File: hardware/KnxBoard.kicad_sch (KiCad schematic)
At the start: 40 parts, among them J1 Conn_01x10, J2 Conn_01x12, J3 Conn_01x12, J4 Conn_01x02_Male, U1 NCN5130, U3 STM32L432KCUx, X1 FA-238

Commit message: Start new schematics
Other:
- sheet MCU ports: added DEBUG_JTCK-SWCLK, DEBUG_JTDA-SWO, DEBUG_JTDI, DEBUG_JTMS-SWDIO, DEBUG_UART_RX, DEBUG_UART_TX, KNX_PROG_BTN, KNX_PROG_LED, KNX_RESETB, KNX_SAVEB, KNX_UART_RX, KNX_UART_TX, NRST, RCC_OSC_IN; removed none
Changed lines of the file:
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@@
     (pin "2")
   )
-  (sheet (at 231.14 137.16) (size 31.75 19.05) (fields_autoplaced)
+  (sheet (at 130.81 142.24) (size 39.37 35.56) (fields_autoplaced)
     (stroke (width 0.1524) (type solid) (color 0 0 0 0))
     (fill (color 0 0 0 0.0000))
-    (property "Sheet name" "MCU" (id 0) (at 231.14 136.4484 0)
+    (property "Sheet name" "MCU" (id 0) (at 130.81 141.5284 0)
       (effects (font (size 1.27 1.27)) (justify left bottom))
     )
-    (property "Sheet file" "mcu.kicad_sch" (id 1) (at 231.14 156.7946 0)
+    (property "Sheet file" "mcu.kicad_sch" (id 1) (at 130.81 178.3846 0)
       (effects (font (size 1.27 1.27)) (justify left top))
+    )
+    (pin "DEBUG_JTDI" input (at 170.18 146.05 0)
+      (effects (font (size 1.27 1.27)) (justify right))
+    )
+    (pin "KNX_UART_TX" output (at 130.81 146.05 180)
+      (effects (font (size 1.27 1.27)) (justify left))
+    )
+    (pin "KNX_UART_RX" input (at 130.81 149.86 180)
+      (effects (font (size 1.27 1.27)) (justify left))
+    )
+    (pin "DEBUG_UART_TX" output (at 170.18 165.1 0)
+      (effects (font (size 1.27 1.27)) (justify right))
+    )
+    (pin "DEBUG_UART_RX" input (at 170.18 161.29 0)
+      (effects (font (size 1.27 1.27)) (justify right))
+    )
+    (pin "DEBUG_JTMS-SWDIO" bidirectional (at 170.18 149.86 0)
+      (effects (font (size 1.27 1.27)) (justify right))
+    )
+    (pin "DEBUG_JTCK-SWCLK" input (at 170.18 153.67 0)
+      (effects (font (size 1.27 1.27)) (justify right))
+    )
+    (pin "DEBUG_JTDA-SWO" output (at 170.18 157.48 0)
+      (effects (font (size 1.27 1.27)) (justify right))
+    )
+    (pin "RCC_OSC_IN" input (at 130.81 153.67 180)
+      (effects (font (size 1.27 1.27)) (justify left))
+    )
+    (pin "KNX_PROG_BTN" input (at 130.81 165.1 180)
+      (effects (font (size 1.27 1.27)) (justify left))
+    )
+    (pin "KNX_PROG_LED" output (at 130.81 168.91 180)
+      (effects (font (size 1.27 1.27)) (justify left))
+    )
+    (pin "KNX_SAVEB" input (at 130.81 157.48 180)
+      (effects (font (size 1.27 1.27)) (justify left))
+    )
+    (pin "NRST" input (at 130.81 175.26 180)
+      (effects (font (size 1.27 1.27)) (justify left))
+    )
+    (pin "KNX_RESETB" input (at 130.81 161.29 180)
+      (effects (font (size 1.27 1.27)) (justify left))
     )
   )
@@
       (reference "#PWR0124") (unit 1) (value "+3.3V") (footprint "")
     )
+    (path "/d8441614-dec4-4bc1-b184-c502a3d79ed5/03d27323-09b9-4b11-a017-9b5707a4dd98"
+      (reference "#PWR?") (unit 1) (value "GNDREF") (footprint "")
+    )
+    (path "/d8441614-dec4-4bc1-b184-c502a3d79ed5/0e9598fb-406f-4d4d-b9a8-c71195fe8ca0"
+      (reference "#PWR?") (unit 1) (value "+3.3V") (footprint "")
+    )
+    (path "/d8441614-dec4-4bc1-b184-c502a3d79ed5/3343c915-cf9e-405b-b8b0-f09759c8714d"
+      (reference "#PWR?") (unit 1) (value "GNDREF") (footprint "")
+    )
+    (path "/d8441614-dec4-4bc1-b184-c502a3d79ed5/3be508aa-8a93-4fde-9c22-a5b8008e5c2e"
+      (reference "#PWR?") (unit 1) (value "GNDREF") (footprint "")
+    )
+    (path "/d8441614-dec4-4bc1-b184-c502a3d79ed5/7b38bb45-3f6f-4e1e-a07e-f7739b04601c"
+      (reference "#PWR?") (unit 1) (value "+3.3V") (footprint "")
+    )
+    (path "/d8441614-dec4-4bc1-b184-c502a3d79ed5/a6da1779-828c-48b4-a087-8262a42e5001"
+      (reference "#PWR?") (unit 1) (value "GNDREF") (footprint "")
+    )
+    (path "/d8441614-dec4-4bc1-b184-c502a3d79ed5/b25d33ec-3885-48d4-84ad-c25564664654"
+      (reference "#PWR?") (unit 1) (value "GNDREF") (footprint "")
+    )
+    (path "/d8441614-dec4-4bc1-b184-c502a3d79ed5/0dea2631-b9f1-4451-83e1-0bf67fac2912"
+      (reference "B1") (unit 1) (value "Reset") (footprint "")
+    )
     (path "/00000000-0000-0000-0000-00006184f7b9"
       (reference "C1") (unit 1) (value "47nF 50V") (footprint "Capacitor_SMD:C_0603_1608Metric")
@@
       (reference "C2") (unit 1) (value "220nF 50V") (footprint "Capacitor_SMD:C_0603_1608Metric")
     )
+    (path "/d8441614-dec4-4bc1-b184-c502a3d79ed5/ed583750-47fe-4327-89c8-ba86b7af17a1"
+      (reference "C2") (unit 1) (value "10uF") (footprint "")
+    )
     (path "/00000000-0000-0000-0000-0000618508bd"
       (reference "C3") (unit 1) (value "100nF 50V") (footprint "Capacitor_SMD:C_0603_1608Metric")
     )
+    (path "/d8441614-dec4-4bc1-b184-c502a3d79ed5/de02d626-c6a9-4a11-a470-5f7c3b547a04"
+      (reference "C3_25") (unit 1) (value "100nF") (footprint "")
+    )
+    (path "/d8441614-dec4-4bc1-b184-c502a3d79ed5/933de220-4835-475e-b429-30ce2da9a7e1"
+      (reference "C3_36") (unit 1) (value "100nF") (footprint "")
+    )
+    (path "/d8441614-dec4-4bc1-b184-c502a3d79ed5/f1ce25fb-e741-4020-b5e8-a7f4df1b610b"
+      (reference "C3_48") (unit 1) (value "100nF") (footprint "")
+    )
     (path "/00000000-0000-0000-0000-00006186317f"
       (reference "C4") (unit 1) (value "100uF 35V") (footprint "Capacitor_SMD:CP_Elec_6.3x7.7")
     )
+    (path "/d8441614-dec4-4bc1-b184-c502a3d79ed5/48cdbdf2-3cea-4abb-8f0a-a74466c9c644"
+      (reference "C4") (unit 1) (value "1uF") (footprint "")
+    )
     (path "/00000000-0000-0000-0000-00006186f111"
       (reference "C5") (unit 1) (value "100nF 6.3V") (footprint "Capacitor_SMD:C_0603_1608Metric")
     )
+    (path "/d8441614-dec4-4bc1-b184-c502a3d79ed5/97e619e0-9643-4a02-b982-345810d00de5"
+      (reference "C5_9") (unit 1) (value "100nF") (footprint "")
+    )
     (path "/00000000-0000-0000-0000-00006186bb40"
       (reference "C6") (unit 1) (value "100nF 6.3V") (footprint "Capacitor_SMD:C_0603_1608Metric")
@@
       (reference "C11") (unit 1) (value "10uF 6.3V ESR < 0.1ohm") (footprint "Capacitor_SMD:C_0805_2012Metric")
     )
+    (path "/d8441614-dec4-4bc1-b184-c502a3d79ed5/96b13407-7e12-4054-b229-f3f0cc548ef8"
+      (reference "C17") (unit 1) (value "100 nF") (footprint "")
+    )
     (path "/00000000-0000-0000-0000-0000619333de"
       (reference "C20") (unit 1) (value "100nF 6.3V") (footprint "Capacitor_SMD:C_0603_1608Metric")
@@
       (reference "C41") (unit 1) (value "1uF 35V ESR < 2ohm") (footprint "Capacitor_SMD:C_0603_1608Metric")
     )
+    (path "/d8441614-dec4-4bc1-b184-c502a3d79ed5/8de7da5f-7df4-40b3-a4bc-ad510060c643"
+      (reference "D0") (unit 1) (value "D_Zener") (footprint "")
+    )
     (path "/00000000-0000-0000-0000-00006184e20b"
       (reference "D1") (unit 1) (value "SS16") (footprint "Diode_SMD:D_SMA")
@@
       (reference "J4") (unit 1) (value "Conn_01x02_Male") (footprint "KnxBoard:KNX_Connector")
     )
+    (path "/d8441614-dec4-4bc1-b184-c502a3d79ed5/fc0c20c5-9ece-4d81-a60c-9e53f7381e41"
+      (reference "JP0") (unit 1) (value "Bootloader") (footprint "")
+    )
+    (path "/d8441614-dec4-4bc1-b184-c502a3d79ed5/22f1cb52-4883-4437-8049-9308b42419f9"
+      (reference "JP1") (unit 1) (value "Bootflash") (footprint "")
+    )
+    (path "/d8441614-dec4-4bc1-b184-c502a3d79ed5/f88a27cb-f856-46c2-87da-e841ed3ef555"
+      (reference "JP2") (unit 1) (value "RESETB_NRST") (footprint "")
+    )
     (path "/00000000-0000-0000-0000-0000618a5317"
       (reference "L1") (unit 1) (value "220uH") (footprint "Inductor_SMD:L_1008_2520Metric")
@@
       (reference "SwReset1") (unit 1) (value "SW_Push") (footprint "Button_Switch_SMD:SW_SPST_SKQG_WithStem")
     )
+    (path "/d8441614-dec4-4bc1-b184-c502a3d79ed5/ea06bc96-3cff-45c0-bbf2-79a6c8f72bbc"
+      (reference "U0") (unit 1) (value "STM32U575CIU6Q") (footprint "KnxBoard:STM32U575CIU6Q")
+    )
     (path "/00000000-0000-0000-0000-00006184ba14"
       (reference "U1") (unit 1) (value "NCN5130") (footprint "Package_DFN_QFN:QFN-40-1EP_6x6mm_P0.5mm_EP4.6x4.6mm_ThermalVias")
@@
       (reference "U3") (unit 1) (value "STM32L432KCUx") (footprint "Package_DFN_QFN:QFN-32-1EP_5x5mm_P0.5mm_EP3.45x3.45mm_ThermalVias")
     )
-    (path "/d8441614-dec4-4bc1-b184-c502a3d79ed5/ea06bc96-3cff-45c0-bbf2-79a6c8f72bbc"
-      (reference "U?") (unit 1) (value "STM32U575CIU6Q") (footprint "KnxBoard:STM32U575CIU6Q")
-    )
     (path "/00000000-0000-0000-0000-0000618e2a33"

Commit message: Work in progress
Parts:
- removed C1: 47nF 50V, Capacitor_SMD:C_0603_1608Metric, symbol Device:C
- removed C10, C11, C22: 10uF 6.3V ESR < 0.1ohm, Capacitor_SMD:C_0805_2012Metric, symbol Device:C
- removed C2: 220nF 50V, Capacitor_SMD:C_0603_1608Metric, symbol Device:C
- removed C20, C21, C23, C5, C6: 100nF 6.3V, Capacitor_SMD:C_0603_1608Metric, symbol Device:C
- removed C3: 100nF 50V, Capacitor_SMD:C_0603_1608Metric, symbol Device:C
- removed C4: 100uF 35V, Capacitor_SMD:CP_Elec_6.3x7.7, symbol KnxBoard-rescue:CP-Device
- removed C41: 1uF 35V ESR < 2ohm, Capacitor_SMD:C_0603_1608Metric, symbol Device:C
- removed C8, C9: 10pF 6.3V, Capacitor_SMD:C_0603_1608Metric, symbol Device:C
- removed D1: SS16, Diode_SMD:D_SMA, symbol Device:D
- removed D2: 1SMA40CA, Diode_SMD:D_SMA, symbol KnxBoard-rescue:D_TVS_ALT-Device
- removed J2, J3: Conn_01x12, Connector_PinHeader_2.54mm:PinHeader_1x12_P2.54mm_Vertical, symbol Connector_Generic:Conn_01x12
- removed L1, L2, L3: 220uH, Inductor_SMD:L_1008_2520Metric, symbol Device:L
- removed R1: 27R 1W, Resistor_SMD:R_0612_1632Metric, symbol Device:R
- removed R2, R3: 1R 1/16W, Resistor_SMD:R_0603_1608Metric, symbol Device:R
- removed R20: 10K 1/16w, Resistor_SMD:R_0603_1608Metric, symbol Device:R
- removed R22, R6: NOTMOUNT, Resistor_SMD:R_0603_1608Metric, symbol Device:R
- removed R4: 56K 1/16w, Resistor_SMD:R_0603_1608Metric, symbol Device:R
- removed R5: 499K 1/16w, Resistor_SMD:R_0603_1608Metric, symbol Device:R
- removed R7: 0, Resistor_SMD:R_0603_1608Metric, symbol Device:R
- removed SwProg1, SwReset1: SW_Push, Button_Switch_SMD:SW_SPST_SKQG_WithStem, symbol Switch:SW_Push
- removed U1: NCN5130, Package_DFN_QFN:QFN-40-1EP_6x6mm_P0.5mm_EP4.6x4.6mm_ThermalVias, symbol KNX_NCN5130:NCN5130
- removed U3: STM32L432KCUx, Package_DFN_QFN:QFN-32-1EP_5x5mm_P0.5mm_EP3.45x3.45mm_ThermalVias, symbol MCU_ST_STM32L4:STM32L432KCUx
- removed X1: FA-238, Crystal:Crystal_SMD_SeikoEpson_FA238-4Pin_3.2x2.5mm, symbol Device:Crystal_GND24
- added B2: KNX_PROG, Button_Switch_SMD:SW_SPST_SKQG_WithStem, symbol Switch:SW_MEC_5E
- added C18: 100nF 6.3V, Capacitor_SMD:C_0603_1608Metric_Pad1.08x0.95mm_HandSolder, symbol Device:C
- added J2, J3: Conn_01x14, Connector_PinHeader_2.54mm:PinHeader_1x14_P2.54mm_Vertical, symbol Connector_Generic:Conn_01x14
- added JP3: PWR_KNX_MCU, Jumper:SolderJumper-2_P1.3mm_Open_TrianglePad1.0x1.5mm, symbol Jumper:SolderJumper_2_Open
- added TP1: KNX_RXD, TestPoint:TestPoint_Pad_D1.5mm, symbol Connector:TestPoint
- added TP2: KNX_TXD, TestPoint:TestPoint_Pad_D1.5mm, symbol Connector:TestPoint
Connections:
- net MCO is gone; now on net MCU/DEBUG_UART_TX: J1.8 (Pin_8)
- net RXD is gone; now on net GNDREF: J1.10 (Pin_10)
- net SWCLK is gone; now on net MCU/DEBUG_JTCK-SWCLK: J1.5 (Pin_5)
- net SWDIO is gone; now on net MCU/DEBUG_UART_RX: J1.7 (Pin_7)
- net TXD is gone; now on net NRST: J1.9 (Pin_9)
- net UART_RX is gone; now on net MCU/DEBUG_JTDI: J1.3 (Pin_3)
- net UART_TX is gone; now on net MCU/DEBUG_JTDA-SWO: J1.6 (Pin_6)
- net +12V: now also J2.1 (Pin_1)
- net CLK16: now also J3.4 (Pin_4)
- net Led: now also R21.1, J3.1 (Pin_1); no longer LD1.2 (A), R21.2
- net MCU/DEBUG_JTMS-SWDIO: now also J1.4 (Pin_4)
- net NRST: now also J3.6 (Pin_6); no longer J1.4 (Pin_4)
- net Prog: now also B2.1, B2.2, C18.1, J3.2 (Pin_2)
- net VDD: now also J2.3 (Pin_3)
- net GND renamed GNDREF
- net GNDREF: now also B2.3 (K), B2.4 (A), C18.2, J2.2 (Pin_2); no longer J4.2 (Pin_2)
- net KNX+ renamed KNXIFACE/KNX+
- new net: LD1.2 (A), R21.2
- new net KNXIFACE/KNX-: J4.2 (Pin_2)
- new net KNXIFACE/KNX_RXD: TP1.1
- new net KNXIFACE/KNX_TXD: TP2.1
- new net KNXIFACE/KNX_V3.3: JP3.2 (B)
- new net KNX_RESETB: J3.5 (Pin_5)
- new net KNX_SAVEB: J3.3 (Pin_3)
- new net MCU/MCU_V33: JP3.1 (A)
- new net MCU/PA0: J3.7 (Pin_7)
- new net MCU/PA1: J3.8 (Pin_8)
- new net MCU/PA11: J2.11 (Pin_11)
- new net MCU/PA12: J2.10 (Pin_10)
- new net MCU/PA4: J3.9 (Pin_9)
- new net MCU/PA5: J3.10 (Pin_10)
- new net MCU/PA6: J3.11 (Pin_11)
- new net MCU/PA7: J3.12 (Pin_12)
- new net MCU/PA8: J2.7 (Pin_7)
- new net MCU/PB0: J3.13 (Pin_13)
- new net MCU/PB1: J3.14 (Pin_14)
- new net MCU/PB13: J2.14 (Pin_14)
- new net MCU/PB14: J2.13 (Pin_13)
- new net MCU/PB15: J2.12 (Pin_12)
- new net MCU/PB4: J2.9 (Pin_9)
- new net MCU/PB5: J2.8 (Pin_8)
- new net MCU/PB6: J2.6 (Pin_6)
- new net MCU/PB7: J2.5 (Pin_5)
- new net MCU/PB8: J2.4 (Pin_4)
- no-connect marks 2 -> 0
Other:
- added sheet KNXIFACE (knxncn.kicad_sch)
- sheet MCU ports: added MCU_GND, MCU_V33, PA0, PA1, PA11, PA12, PA4, PA5, PA6, PA7, PA8, PB0, PB1, PB13, PB14, PB15, PB4, PB5, PB6, PB7, PB8; removed none
- moved on the sheet: J1, J4, LD1, R21

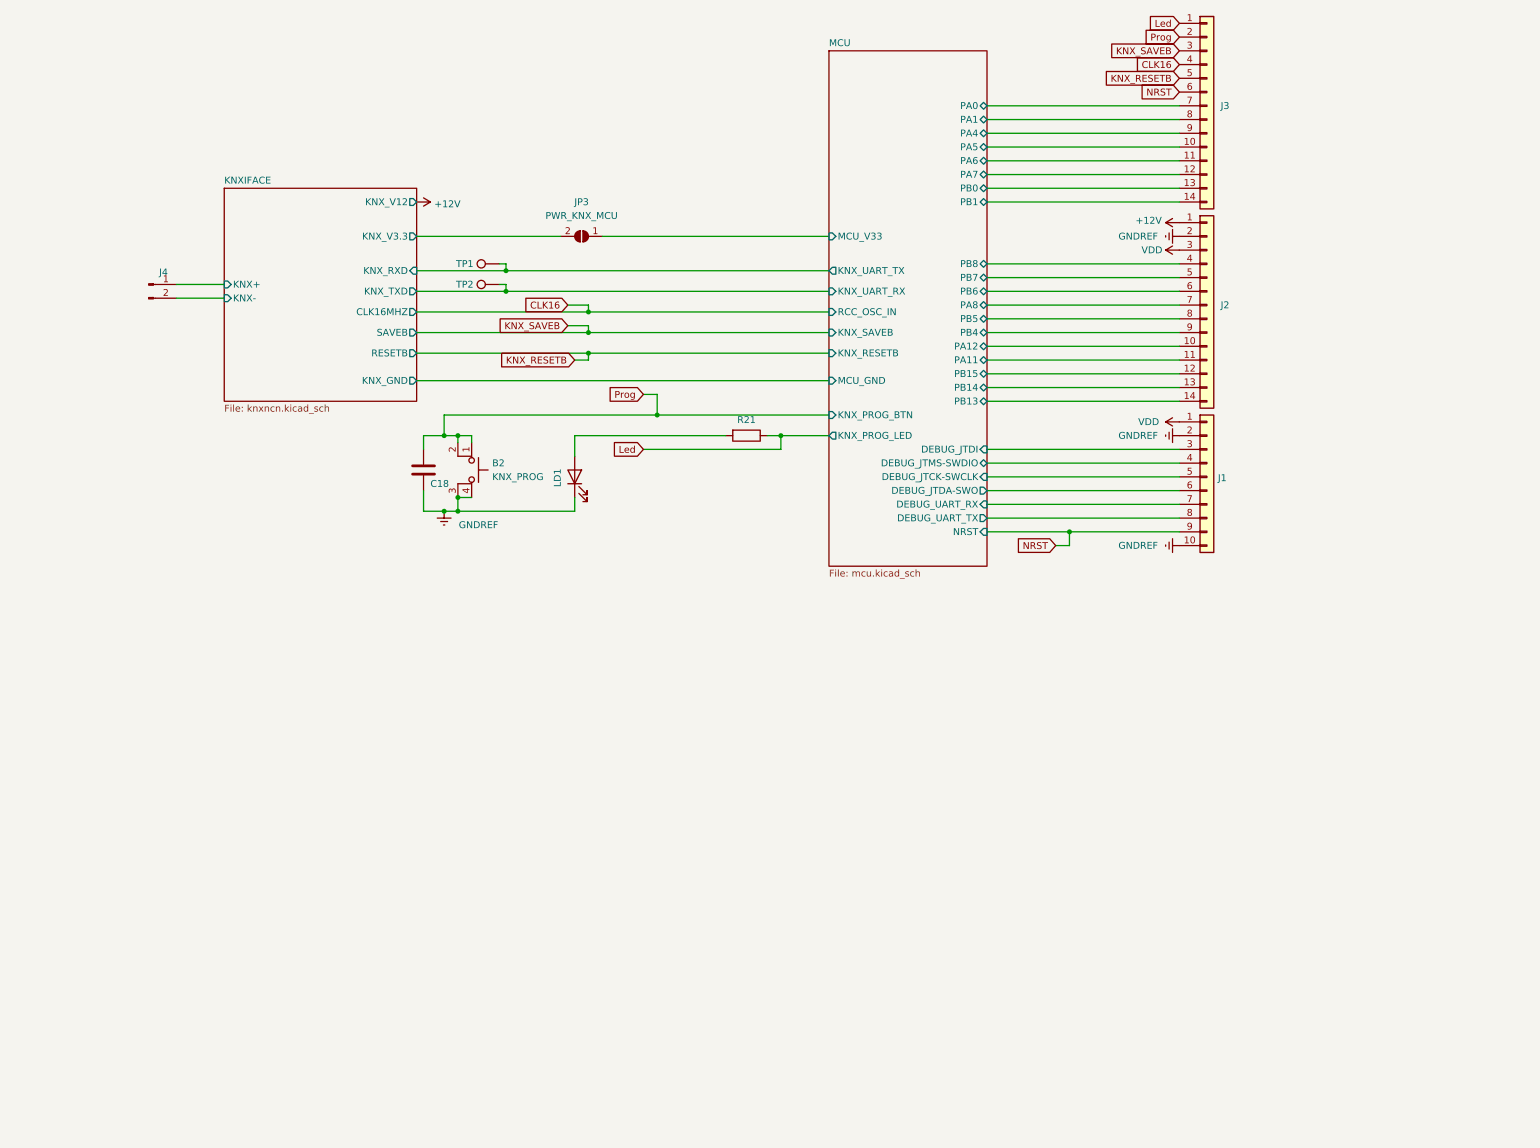
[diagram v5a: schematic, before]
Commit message: Switch to STM32U575CIT6
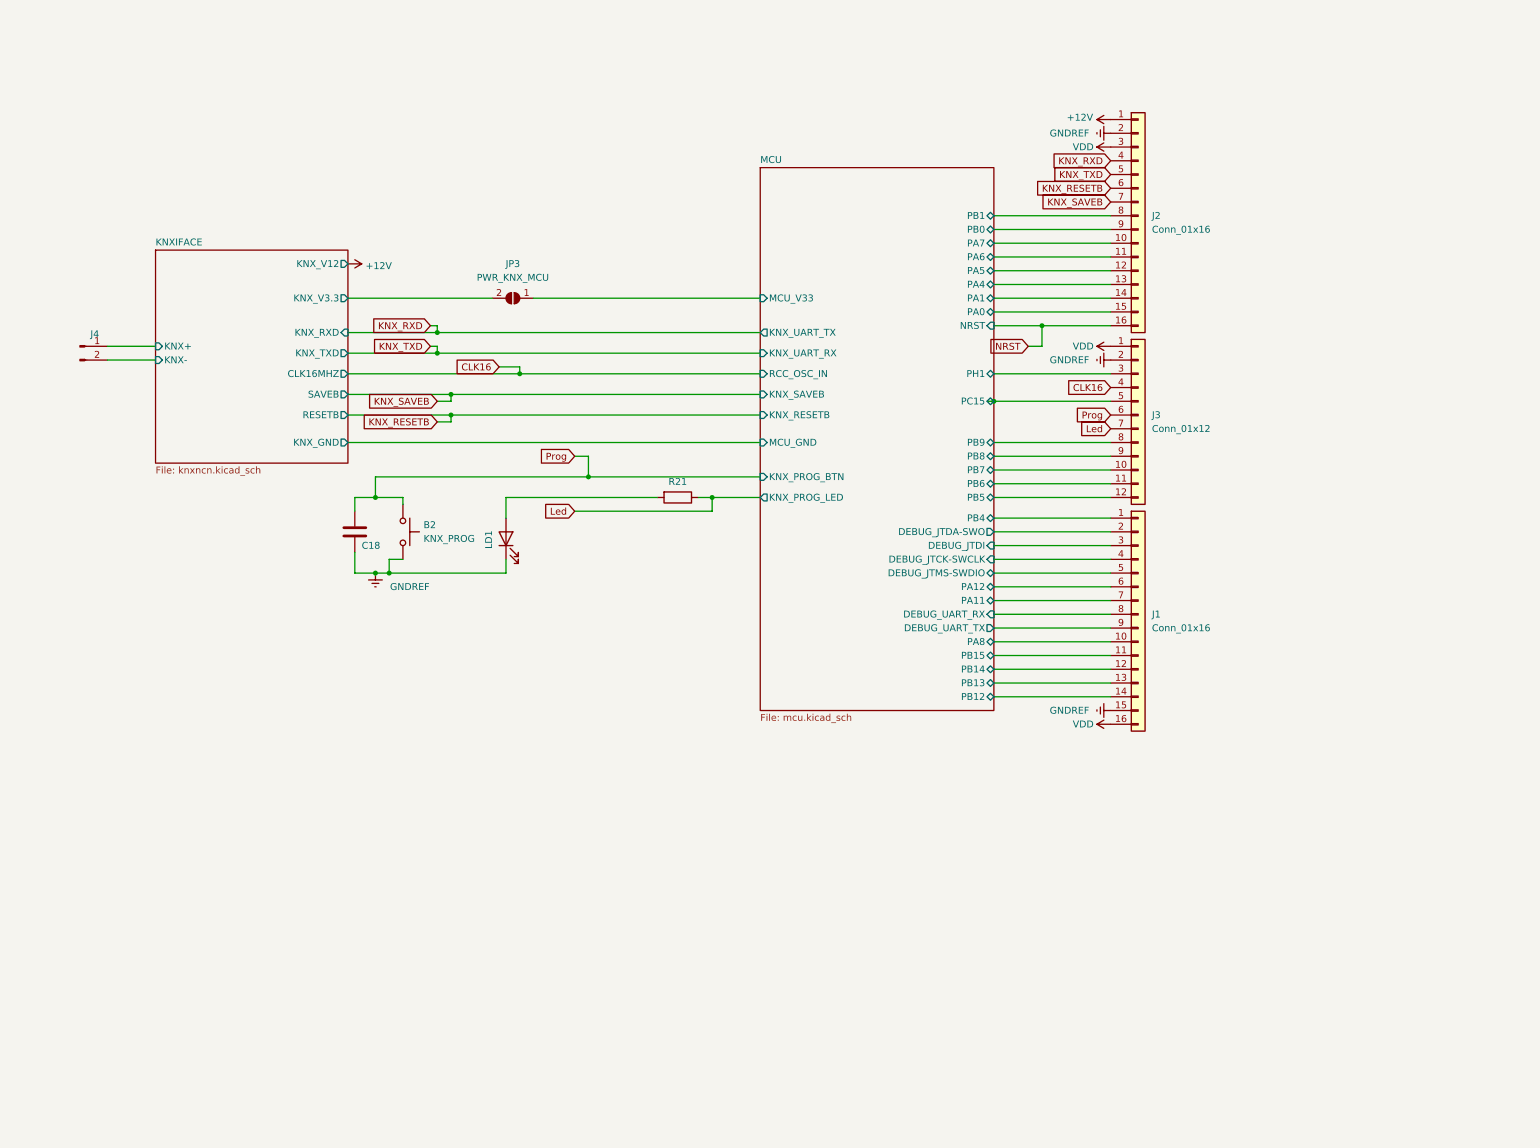
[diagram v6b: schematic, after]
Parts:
- removed B2: KNX_PROG, Button_Switch_SMD:SW_SPST_SKQG_WithStem, symbol Switch:SW_MEC_5E
- removed J1: Conn_01x10, Connector_PinHeader_1.27mm:PinHeader_2x05_P1.27mm_Vertical, symbol Connector_Generic:Conn_01x10
- removed J2, J3: Conn_01x14, Connector_PinHeader_2.54mm:PinHeader_1x14_P2.54mm_Vertical, symbol Connector_Generic:Conn_01x14
- removed TP1: KNX_RXD, TestPoint:TestPoint_Pad_D1.5mm, symbol Connector:TestPoint
- removed TP2: KNX_TXD, TestPoint:TestPoint_Pad_D1.5mm, symbol Connector:TestPoint
- added B2: KNX_PROG, Button_Switch_SMD:SW_SPST_SKQG_WithStem, symbol Switch:SW_Push
- added J1, J2: Conn_01x16, Connector_PinHeader_2.54mm:PinHeader_1x16_P2.54mm_Vertical, symbol Connector_Generic:Conn_01x16
- added J3: Conn_01x12, Connector_PinHeader_2.54mm:PinHeader_1x12_P2.54mm_Vertical, symbol Connector_Generic:Conn_01x12
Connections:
- net +12V: now also J2.1 (Pin_1)
- net CLK16: now also J3.4 (Pin_4)
- net GNDREF: now also B2.2, J1.15 (Pin_15), J2.2 (Pin_2), J3.2 (Pin_2)
- net KNX_RESETB: now also J2.6 (Pin_6)
- net KNX_SAVEB: now also J2.7 (Pin_7)
- net Led: now also J3.7 (Pin_7)
- net MCU/DEBUG_JTCK-SWCLK: now also J1.4 (Pin_4)
- net MCU/DEBUG_JTDA-SWO: now also J1.2 (Pin_2)
- net MCU/DEBUG_JTDI: now also J1.3 (Pin_3)
- net MCU/DEBUG_JTMS-SWDIO: now also J1.5 (Pin_5)
- net MCU/DEBUG_UART_RX: now also J1.8 (Pin_8)
- net MCU/DEBUG_UART_TX: now also J1.9 (Pin_9)
- net MCU/PA0: now also J2.15 (Pin_15)
- net MCU/PA1: now also J2.14 (Pin_14)
- net MCU/PA11: now also J1.7 (Pin_7)
- net MCU/PA12: now also J1.6 (Pin_6)
- net MCU/PA4: now also J2.13 (Pin_13)
- net MCU/PA5: now also J2.12 (Pin_12)
- net MCU/PA6: now also J2.11 (Pin_11)
- net MCU/PA7: now also J2.10 (Pin_10)
- net MCU/PA8: now also J1.10 (Pin_10)
- net MCU/PB0: now also J2.9 (Pin_9)
- net MCU/PB1: now also J2.8 (Pin_8)
- net MCU/PB13: now also J1.13 (Pin_13)
- net MCU/PB14: now also J1.12 (Pin_12)
- net MCU/PB15: now also J1.11 (Pin_11)
- net MCU/PB4: now also J1.1 (Pin_1)
- net MCU/PB5: now also J3.12 (Pin_12)
- net MCU/PB6: now also J3.11 (Pin_11)
- net MCU/PB7: now also J3.10 (Pin_10)
- net MCU/PB8: now also J3.9 (Pin_9)
- net NRST: now also J2.16 (Pin_16)
- net Prog: now also B2.1, J3.6 (Pin_6)
- net VDD: now also J1.16 (Pin_16), J2.3 (Pin_3), J3.1 (Pin_1)
- new net KNX_RXD: J2.4 (Pin_4)
- new net KNX_TXD: J2.5 (Pin_5)
- new net MCU/PB12: J1.14 (Pin_14)
- new net MCU/PB9: J3.8 (Pin_8)
- new net MCU/PC15: J3.5 (Pin_5)
- new net MCU/PH1: J3.3 (Pin_3)
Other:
- sheet MCU ports: added PB12, PB9, PC15, PH1; removed none
- moved on the sheet: C18, J4, JP3, LD1, R21
